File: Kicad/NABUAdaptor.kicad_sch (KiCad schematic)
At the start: 103 parts, among them J1 Conn_01x04, J2 DIN-5_180degree, J3 Conn_01x09, J4 Conn_01x05, U1 74LS164, U10 UA9638CD, U11 UA9637, U12 74LS164, U13 74LS164, U14 74LS04, U15 74LS74, U16 N8X60, U17 2114, U18 2114, U19 LM339, U2 74LS30, U20 74LS164, U21 74LS86, U22 74LS74, U23 74LS00, U24 74LS04, U25 74LS00, U26 74LS74, U27 74LS00, U28 74LS74, U29 74LS74, U3 74LS27, U30 74LS02, U31 MC6805P2, U32 74LS74, U33 74HCU04, U4 74LS164, U5 PAL16R6 (ID PAL), U6 74LS374, U7 74LS373, U8 3k3, U9 TR1865PL, Y1 3.579545MHz

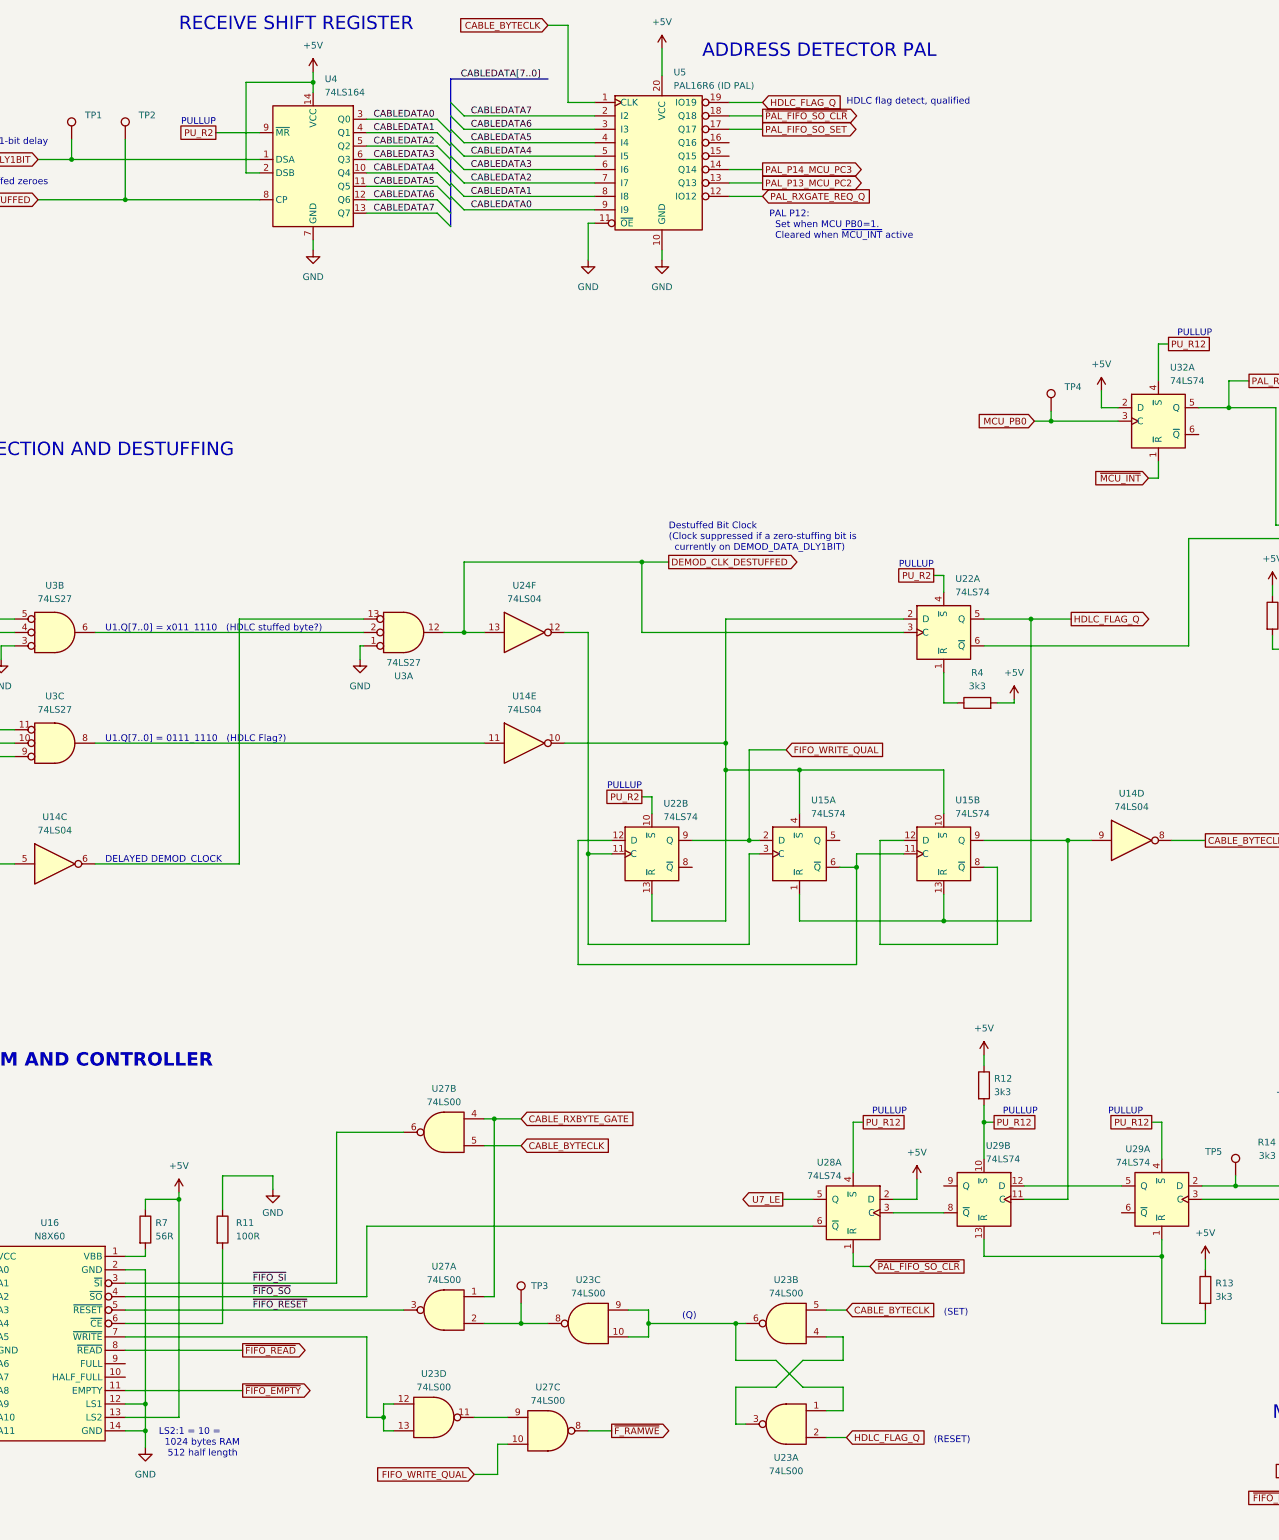
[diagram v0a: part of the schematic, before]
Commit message: sch: HDLC_FLAG_Q is inverted
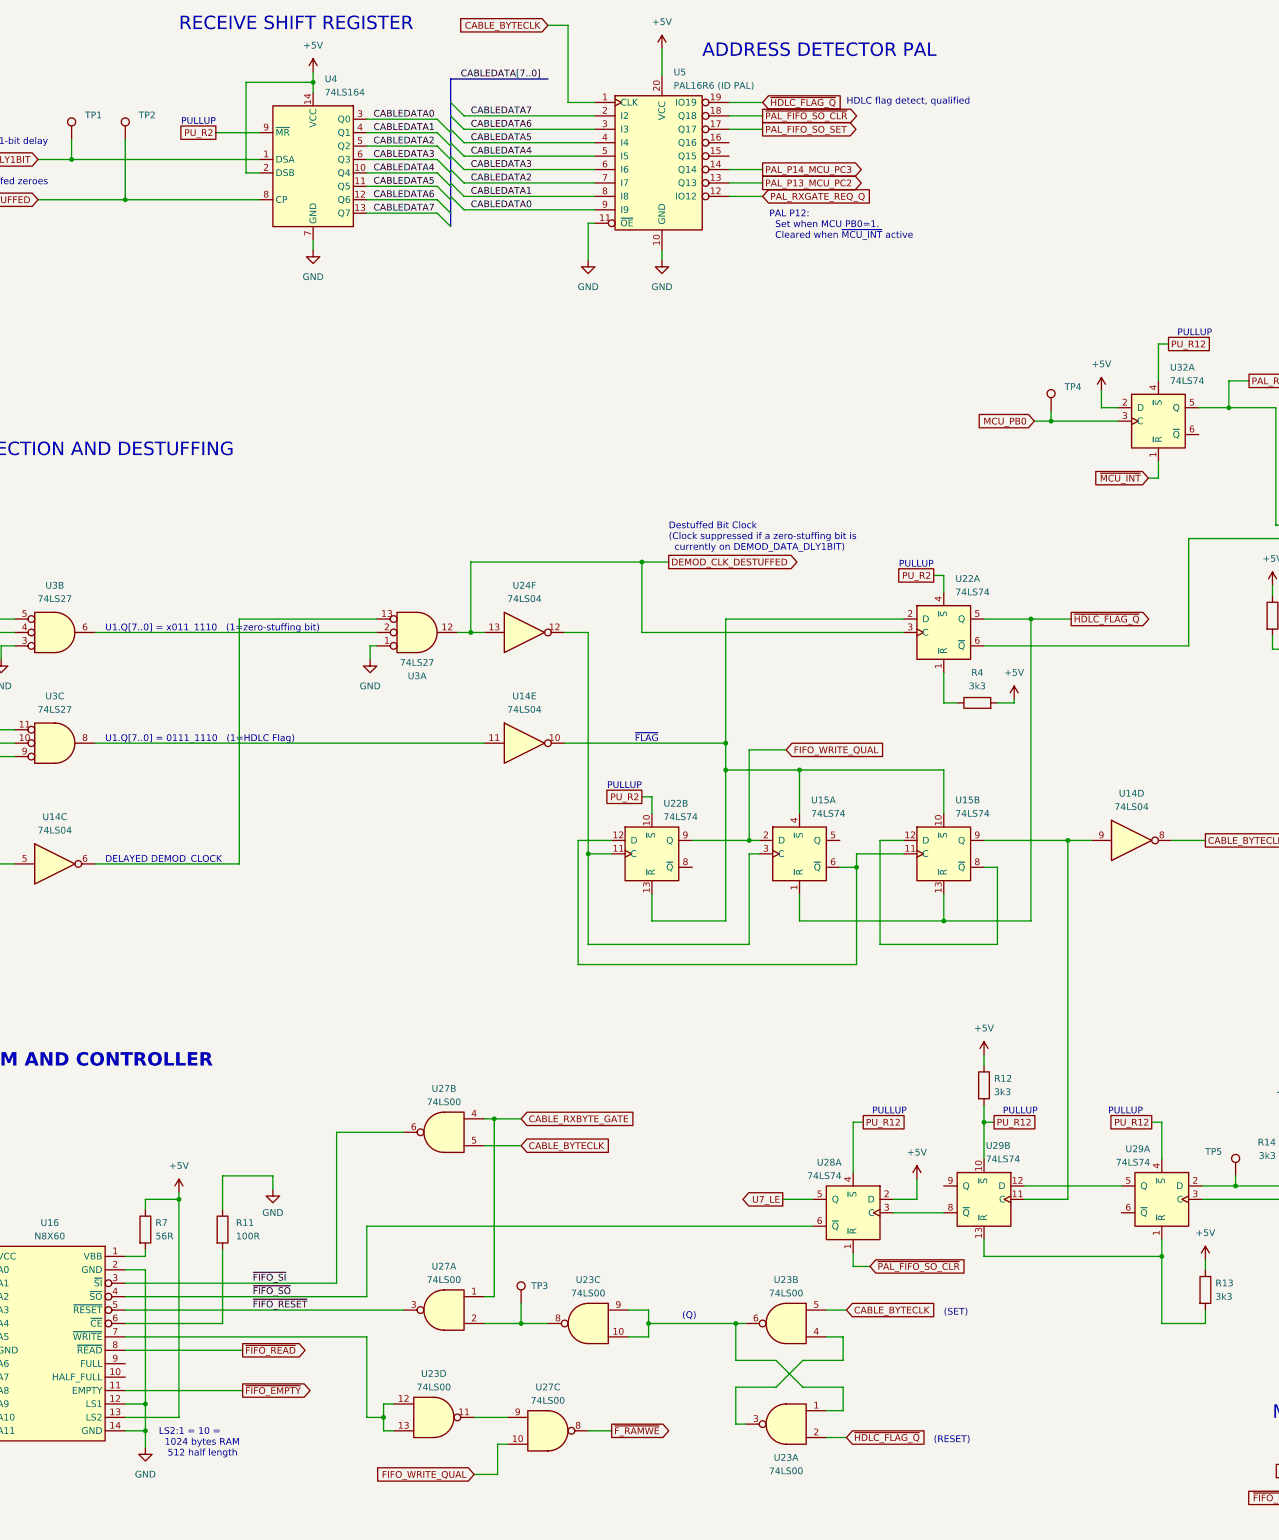
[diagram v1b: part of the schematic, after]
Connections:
- net HDLC_FLAG_Q renamed ~{HDLC_FLAG_Q}
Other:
- note added: "U1.Q[7..0] = 0111_1110 (1=HDLC Flag)"
- note added: "U1.Q[7..0] = x011_1110 (1=zero-stuffing bit)"
- note added: "~{FLAG}"
- note removed: "U1.Q[7..0] = 0111_1110 (HDLC Flag?)"
- note removed: "U1.Q[7..0] = x011_1110 (HDLC stuffed byte?)"
- moved on the sheet: U3A
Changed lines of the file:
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@@
   (junction (at 88.9 144.145) (diameter 0) (color 0 0 0 0)
   )
-  (junction (at 361.95 163.195) (diameter 0) (color 0 0 0 0)
-  )
   (junction (at 687.705 556.895) (diameter 0) (color 0 0 0 0)
   )
@@
   (junction (at 775.335 63.5) (diameter 0) (color 0 0 0 0)
   )
+  (junction (at 363.22 163.195) (diameter 0) (color 0 0 0 0)
+  )
   (junction (at 687.705 525.145) (diameter 0) (color 0 0 0 0)
   )
@@
     (stroke (width 0) (type default))
   )
-  (wire (pts (xy 361.95 149.86) (xy 395.605 149.86))
+  (wire (pts (xy 363.22 149.86) (xy 395.605 149.86))
     (stroke (width 0) (type default))
   )
@@
     (stroke (width 0) (type default))
   )
-  (wire (pts (xy 292.1 163.195) (xy 342.9 163.195))
+  (wire (pts (xy 292.1 163.195) (xy 345.44 163.195))
     (stroke (width 0) (type default))
   )
@@
     (stroke (width 0) (type default))
   )
+  (wire (pts (xy 363.22 163.195) (xy 365.76 163.195))
+    (stroke (width 0) (type default))
+  )
   (bus (pts (xy 359.41 68.58) (xy 359.41 67.945))
     (stroke (width 0) (type default))
@@
     (stroke (width 0) (type default))
   )
+  (wire (pts (xy 360.68 163.195) (xy 363.22 163.195))
+    (stroke (width 0) (type default))
+  )
   (wire (pts (xy 301.625 386.08) (xy 301.625 401.32))
     (stroke (width 0) (type default))
@@
     (stroke (width 0) (type default))
   )
-  (wire (pts (xy 361.95 149.86) (xy 361.95 163.195))
+  (wire (pts (xy 363.22 149.86) (xy 363.22 163.195))
     (stroke (width 0) (type default))
   )
@@
     (stroke (width 0) (type default))
   )
-  (wire (pts (xy 358.14 163.195) (xy 361.95 163.195))
-    (stroke (width 0) (type default))
-  )
   (wire (pts (xy 687.705 525.145) (xy 687.705 538.48))
     (stroke (width 0) (type default))
@@
     (stroke (width 0) (type default))
   )
-  (wire (pts (xy 342.9 165.735) (xy 342.265 165.735))
+  (wire (pts (xy 345.44 165.735) (xy 344.17 165.735))
     (stroke (width 0) (type default))
   )
@@
     (stroke (width 0) (type default))
   )
-  (wire (pts (xy 319.405 160.655) (xy 342.9 160.655))
+  (wire (pts (xy 319.405 160.655) (xy 345.44 160.655))
     (stroke (width 0) (type default))
   )
@@
     (stroke (width 0) (type default))
   )
-  (wire (pts (xy 342.265 165.735) (xy 342.265 168.275))
+  (wire (pts (xy 344.17 165.735) (xy 344.17 168.275))
     (stroke (width 0) (type default))
   )
@@
     (stroke (width 0) (type default))
   )
-  (wire (pts (xy 361.95 163.195) (xy 365.76 163.195))
-    (stroke (width 0) (type default))
-  )
   (wire (pts (xy 333.375 414.02) (xy 347.98 414.02))
     (stroke (width 0) (type default))
@@
     (effects (font (size 1.27 1.27)) (justify right bottom))
   )
+  (text "~{FLAG}" (at 398.78 184.15 0)
+    (effects (font (size 1.27 1.27)) (justify right bottom))
+  )
   (text "PAL P12:\n  Set when MCU PB0=1.\n  Cleared when ~{MCU_INT} active"
     (at 419.735 88.9 0)
@@
     (effects (font (size 1.27 1.27)) (justify right bottom))
   )
-  (text "U1.Q[7..0] = x011_1110   (HDLC stuffed byte?)" (at 294.005 163.195 0)
+  (text "U1.Q[7..0] = x011_1110   (1=zero-stuffing bit)" (at 294.005 163.195 0)
     (effects (font (size 1.27 1.27)) (justify left bottom))
   )
@@
     (effects (font (size 1.27 1.27)) (justify left bottom))
   )
-  (text "U1.Q[7..0] = 0111_1110   (HDLC Flag?)" (at 294.005 184.15 0)
+  (text "U1.Q[7..0] = 0111_1110   (1=HDLC Flag)" (at 294.005 184.15 0)
     (effects (font (size 1.27 1.27)) (justify left bottom))
   )
@@
     )
   )
-  (global_label "HDLC_FLAG_Q" (shape input) (at 434.34 315.595 0) (fields_autoplaced)
+  (global_label "~{HDLC_FLAG_Q}" (shape input) (at 434.34 315.595 0) (fields_autoplaced)
     (effects (font (size 1.27 1.27)) (justify left))
     (property "Intersheetrefs" "${INTERSHEET_REFS}" (at 449.9648 315.595 0)
@@
     )
   )
-  (global_label "HDLC_FLAG_Q" (shape output) (at 476.885 160.655 0) (fields_autoplaced)
+  (global_label "~{HDLC_FLAG_Q}" (shape output) (at 476.885 160.655 0) (fields_autoplaced)
     (effects (font (size 1.27 1.27)) (justify left))
     (property "Intersheetrefs" "${INTERSHEET_REFS}" (at 492.5098 160.655 0)
@@
     )
   )
-  (global_label "HDLC_FLAG_Q" (shape input) (at 418.465 62.865 0) (fields_autoplaced)
+  (global_label "~{HDLC_FLAG_Q}" (shape input) (at 418.465 62.865 0) (fields_autoplaced)
     (effects (font (size 1.27 1.27)) (justify left))
     (property "Intersheetrefs" "${INTERSHEET_REFS}" (at 434.0898 62.865 0)
@@
     )
   )
-  (symbol (lib_id "74xx:74LS27") (at 350.52 163.195 0) (mirror x) (unit 1) (convert 2)
+  (symbol (lib_id "74xx:74LS27") (at 353.06 163.195 0) (mirror x) (unit 1) (convert 2)
     (in_bom yes) (on_board yes) (dnp no) (fields_autoplaced)
-    (property "Reference" "U3" (at 350.52 171.45 0)
+    (property "Reference" "U3" (at 353.06 171.45 0)
       (effects (font (size 1.27 1.27)))
     )
-    (property "Value" "74LS27" (at 350.52 168.91 0)
+    (property "Value" "74LS27" (at 353.06 168.91 0)
       (effects (font (size 1.27 1.27)))
     )
-    (property "Footprint" "" (at 350.52 163.195 0)
+    (property "Footprint" "" (at 353.06 163.195 0)
       (effects (font (size 1.27 1.27)) hide)
     )
-    (property "Datasheet" "http://www.ti.com/lit/gpn/sn74LS27" (at 350.52 163.195 0)
+    (property "Datasheet" "http://www.ti.com/lit/gpn/sn74LS27" (at 353.06 163.195 0)
       (effects (font (size 1.27 1.27)) hide)
     )
@@
     )
   )
-  (symbol (lib_id "power:GND") (at 342.265 168.275 0) (unit 1)
+  (symbol (lib_id "power:GND") (at 344.17 168.275 0) (unit 1)
     (in_bom yes) (on_board yes) (dnp no) (fields_autoplaced)
-    (property "Reference" "#PWR018" (at 342.265 174.625 0)
+    (property "Reference" "#PWR018" (at 344.17 174.625 0)
       (effects (font (size 1.27 1.27)) hide)
     )
-    (property "Value" "GND" (at 342.265 173.355 0)
+    (property "Value" "GND" (at 344.17 173.355 0)
       (effects (font (size 1.27 1.27)))
     )
-    (property "Footprint" "" (at 342.265 168.275 0)
+    (property "Footprint" "" (at 344.17 168.275 0)
       (effects (font (size 1.27 1.27)) hide)
     )
-    (property "Datasheet" "" (at 342.265 168.275 0)
+    (property "Datasheet" "" (at 344.17 168.275 0)
       (effects (font (size 1.27 1.27)) hide)
     )
